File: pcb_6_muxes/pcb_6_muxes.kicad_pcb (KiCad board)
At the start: 2 copper layers, 121.9 x 121.9 mm, 36 parts, among them U1 74HC4051, U2 74HC4051, U3 74HC4051, U4 74HC4051, U5 74HC4051, U6 74HC4051

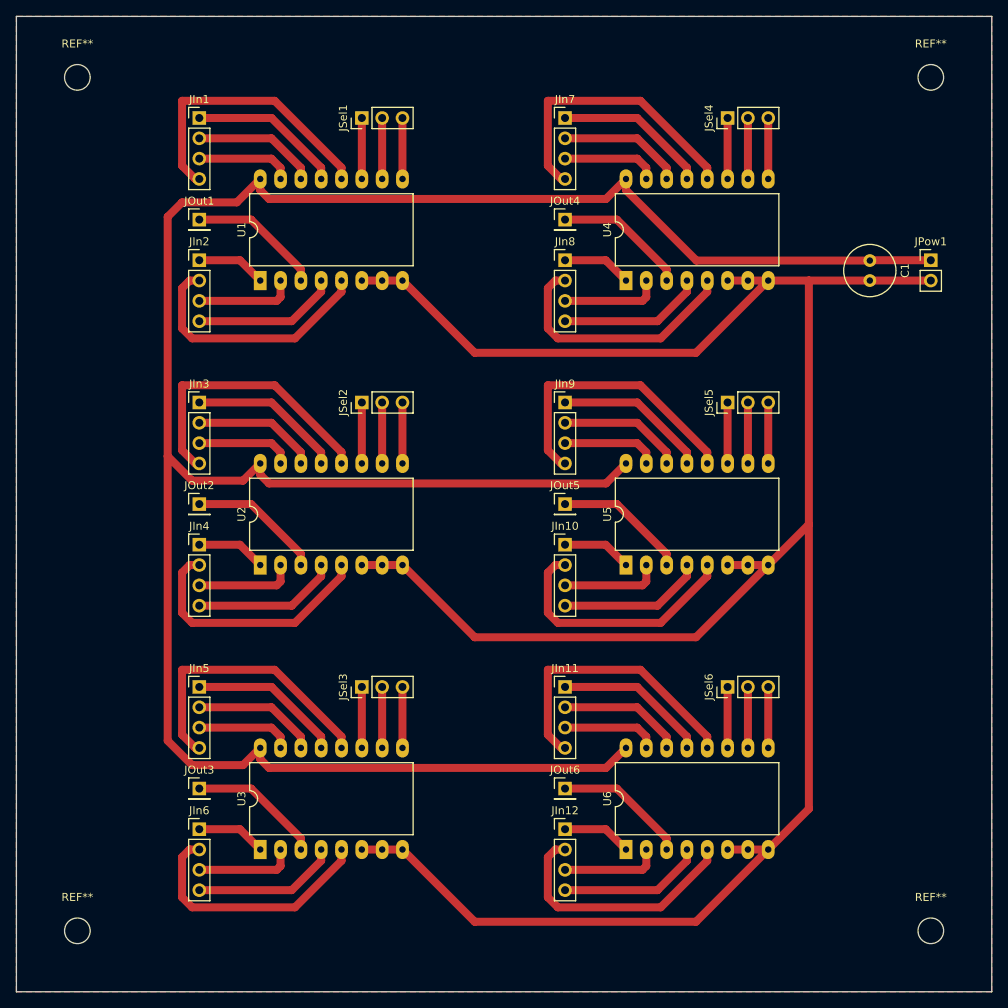
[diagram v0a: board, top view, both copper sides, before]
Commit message: Move copper from top to bottom layer for easier solering on single sided board.
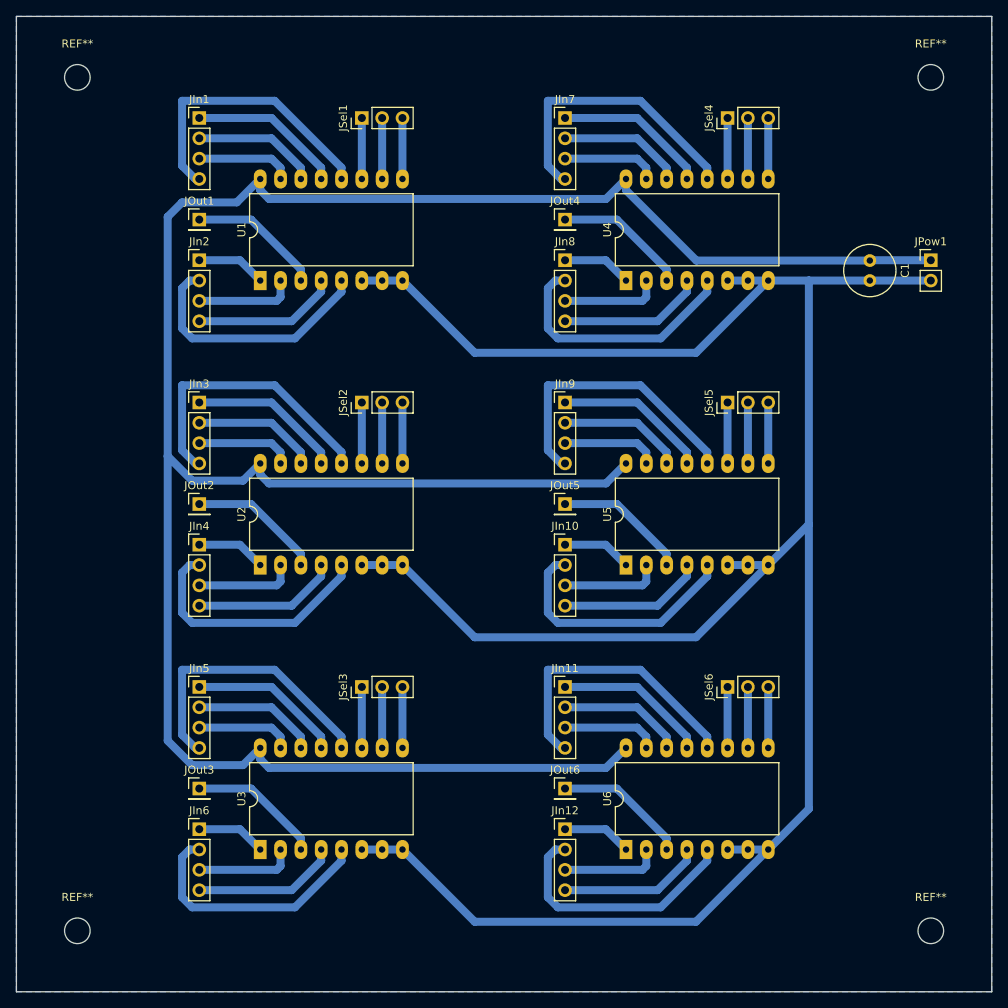
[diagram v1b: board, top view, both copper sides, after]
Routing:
- added copper zone on B.Cu, net GND
- removed copper zone on F.Cu, net GND
